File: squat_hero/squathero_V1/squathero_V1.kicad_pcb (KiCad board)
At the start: 2 copper layers, 36.5 x 31.5 mm, 6 parts, among them U2 AMS1117

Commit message: V1 squat hero
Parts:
- removed FB1: ~, PCM_JLCPCB:FB_0805
- added C1: 1uF, Resistor_SMD:R_0805_2012Metric, F.Cu at (148.9, 115.5)
- added C2: 10nF, Resistor_SMD:R_0805_2012Metric, F.Cu at (146.8, 115.5)
- added C3: 1uF, Resistor_SMD:R_0805_2012Metric, F.Cu at (148.9, 109.8)
- added C4: 1uF, Resistor_SMD:R_0805_2012Metric, F.Cu at (171.1, 94.4)
- added C5: 1uF, Resistor_SMD:R_0805_2012Metric, F.Cu at (166.2, 92.5)
- added D2: Yellow, PCM_JLCPCB:D_0805, F.Cu at (147.4, 122.2)
- added D3: Green, PCM_JLCPCB:D_0805, F.Cu at (167.4, 107.8)
- added D4: Red, PCM_JLCPCB:D_0603, F.Cu at (167.4, 105.8)
- added D5: 1N5819WS, PCM_JLCPCB:D_SOD-323, F.Cu at (160.2, 92.2)
- added D6: 1N5819WS, PCM_JLCPCB:D_SOD-323, F.Cu at (156.0, 96.8)
- added D7: H3V3L10B, PCM_JLCPCB:D_DFN1006-2L, F.Cu at (158.0, 82.2)
- added D8: H3V3L10B, PCM_JLCPCB:D_DFN1006-2L, F.Cu at (158.2, 83.5)
- added FB2: ~, PCM_JLCPCB:FB_0805, F.Cu at (164.0, 92.5)
- added J1: Conn_01x03, Connector_PinSocket_2.54mm:PinSocket_1x03_P2.54mm_Vertical, F.Cu at (132.5, 87.1)
- added J3: Conn_01x02, Connector_PinSocket_2.54mm:PinSocket_1x02_P2.54mm_Vertical, F.Cu at (130.4, 109.4)
- added J4: Conn_01x02, Connector_PinSocket_2.54mm:PinSocket_1x02_P2.54mm_Vertical, F.Cu at (128.2, 99.0)
- added J5: Conn_01x02, Connector_PinSocket_2.54mm:PinSocket_1x02_P2.54mm_Vertical, F.Cu at (155.8, 102.5)
- added Q1: HL2307, PCM_JLCPCB:Q_SOT-23, F.Cu at (135.1, 109.5)
- added Q2: HL2307, PCM_JLCPCB:Q_SOT-23, F.Cu at (132.3, 101.7)
- added Q3: HL2307, PCM_JLCPCB:Q_SOT-23, F.Cu at (159.9, 96.8)
- added R10: 2.5k, Resistor_SMD:R_0805_2012Metric, F.Cu at (164.2, 104.2)
- added R11: 10k, Resistor_SMD:R_0805_2012Metric, F.Cu at (165.3, 96.8)
- added R12: 330, Resistor_SMD:R_0805_2012Metric, F.Cu at (133.2, 93.2)
- added R13: 330, Resistor_SMD:R_0805_2012Metric, F.Cu at (134.5, 91.0)
- added R3: 10k, Resistor_SMD:R_0805_2012Metric, F.Cu at (146.8, 111.8)
- added R4: 4.7k, Resistor_SMD:R_0805_2012Metric, F.Cu at (147.3, 95.2)
- added R5: 4.7k, Resistor_SMD:R_0805_2012Metric, F.Cu at (152.1, 92.6)
- added R6: 10k, Resistor_SMD:R_0805_2012Metric, F.Cu at (139.9, 90.0)
- added R7: 50, Resistor_SMD:R_0805_2012Metric, F.Cu at (152.6, 120.0)
- added R8: 50, Resistor_SMD:R_0805_2012Metric, F.Cu at (147.4, 120.0)
- added R9: 1k, Resistor_SMD:R_0805_2012Metric, F.Cu at (167.4, 110.0)
- added S1: Tactile Button, 160gf, PCM_JLCPCB:SW-SMD_4P-L5.1-W5.1-P3.70-LS6.5-TL-2, F.Cu at (139.8, 84.5)
- added U3: AMS1117-3.3, Package_TO_SOT_SMD:SOT-223-3_TabPin2, F.Cu at (156.0, 111.4)
- added U4: ~, imu:LGA-14_L3.0-W2.5-P0.50-TL_QMI8658A, F.Cu at (150.0, 100.0)
- added U5: TP4057, PCM_JLCPCB:SOT-23-6_L2.9-W1.6-P0.95-LS2.8-BL, F.Cu at (165.5, 100.0)
- added U6: ~, batt_conn:Untitled, F.Cu at (171.0, 100.1)
- D1: value H5VUT1B -> White; footprint PCM_JLCPCB:SOT-143-4_L2.9-W1.3-P1.90-LS2.4-BL-1 -> PCM_JLCPCB:D_0805
- R1, R2: footprint Resistor_SMD:R_0805_2012Metric -> Resistor_SMD:R_0201_0603Metric
- U1: footprint JLCPCB_USB-C:USB-SMD_TYPE-C16PIN-1 -> JLCPCB_USB_FOOTPRINT:USB-SMD_TYPE-C16PIN-1
- U2: value AMS1117 -> ~; footprint PCM_JLCPCB:SOT-223-3_L6.5-W3.4-P2.30-LS7.0-BR -> esp_32:WIFIM-SMD_ESP32-C3-MINI-1
- moved U1 52.3 mm to (164.7, 85.3), turned to 135 degrees
- moved R1 51.8 mm to (169.8, 89.1), turned to -45 degrees
- moved D1 40.2 mm to (152.6, 122.2)
- moved R2 39.9 mm to (169.2, 89.7), turned to -45 degrees
- moved U2 27.0 mm to (150.0, 81.7), turned to 0 degrees
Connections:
- D1 pad 1: /USB_D+ -> Net-(D1-Pad1)
- D1 pad 2: /USB_D- -> /DEBUG_LED1
- U2 pad 2: REG_3.3V -> GND
- U2 pad 3: /+5V -> /+3.3V
- U2 pad 4: REG_3.3V -> unconnected-(U2-NC-Pad4)
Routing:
- net /DEBUG_LED2: track 0.00 -> 56.2 mm, vias 0 -> 2
- net /DEBUG_LED1: track 0.00 -> 55.4 mm, vias 0 -> 2
- net /+5V: track 0.00 -> 39.3 mm
- net /PWM_1: track 0.00 -> 37.0 mm, vias 0 -> 2
- net /PWM_2: track 0.00 -> 36.2 mm, vias 0 -> 2
- net GND: track 0.00 -> 27.4 mm, vias 0 -> 49
- net /+3.3V: track 0.00 -> 25.6 mm, vias 0 -> 13
- net /BATT+: track 0.00 -> 24.2 mm, vias 0 -> 2
- net /I2C_INT1: track 0.00 -> 22.1 mm, vias 0 -> 2
- net /GPI0_10: track 0.00 -> 18.8 mm, vias 0 -> 2
- net /raw_power: track 0.00 -> 18.0 mm
- net /I2C_SCL_1: track 0.00 -> 15.4 mm
- net /I2C_SDA_1: track 0.00 -> 15.3 mm
- net /I2C_INT2: track 0.00 -> 15.1 mm, vias 0 -> 2
- net /GPI0_1: track 0.00 -> 14.0 mm, vias 0 -> 2
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- added copper zone on F.Cu, net /+3.3V
- added copper zone on In2.Cu, net /+3.3V
- added copper zone on In1.Cu, net GND
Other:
- board size 36.5 x 31.5 mm -> 50 x 50 mm
- copper layers 2 -> 4

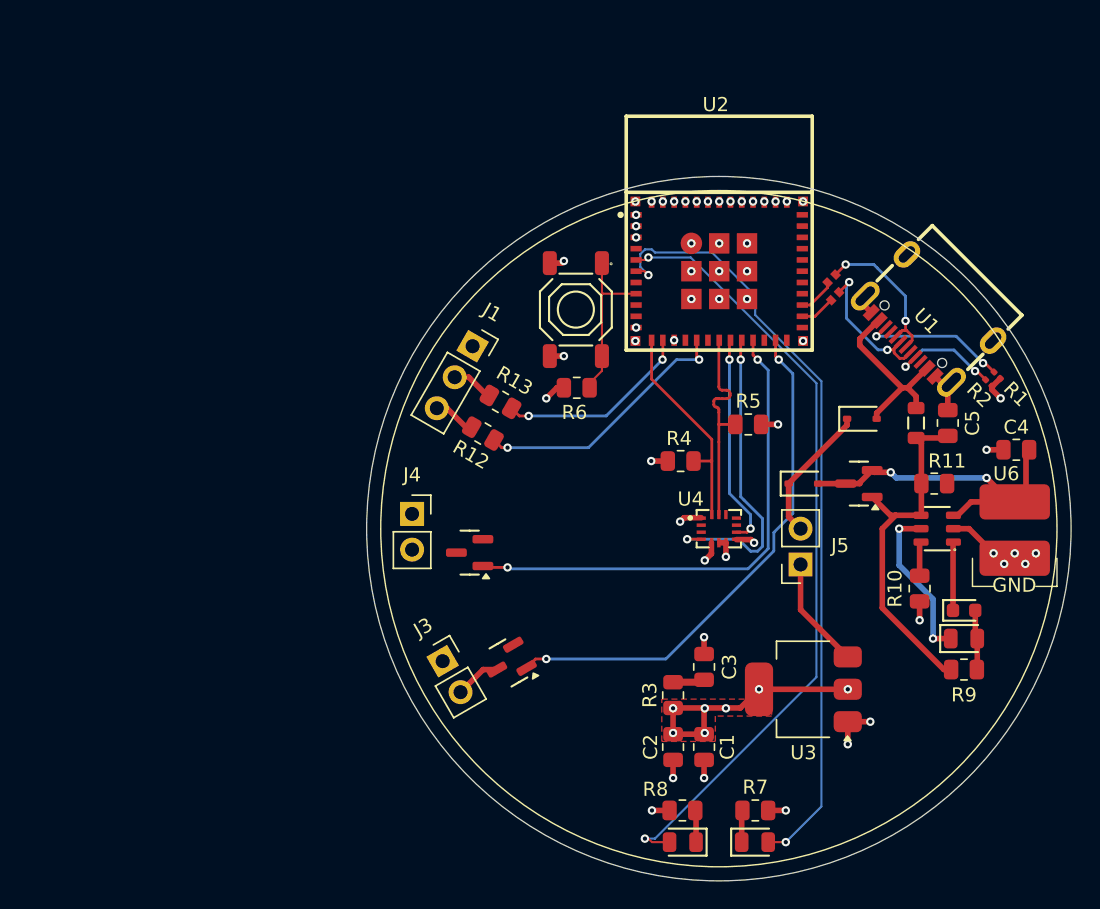
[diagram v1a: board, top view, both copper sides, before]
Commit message: all formatted besides power / BMS
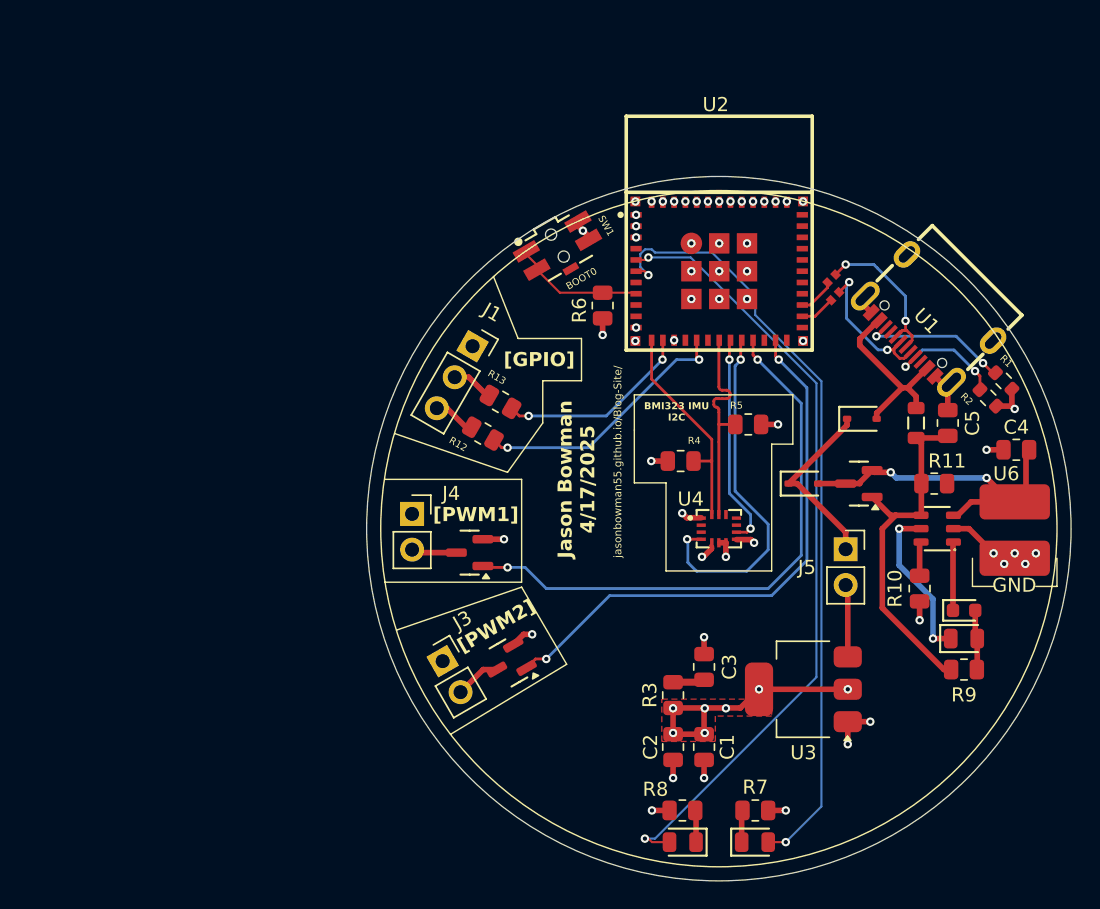
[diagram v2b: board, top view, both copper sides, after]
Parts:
- removed S1: Tactile Button, 160gf, PCM_JLCPCB:SW-SMD_4P-L5.1-W5.1-P3.70-LS6.5-TL-2
- added SW1: ~, Button_Switch_SMD:SW-SMD_4P-L3.5-W3.5_PTS840GKPSMTRLFS, F.Cu at (138.8, 80.4)
- R1, R2: footprint Resistor_SMD:R_0201_0603Metric -> Resistor_SMD:R_0603_1608Metric
- moved R6 6.12 mm to (141.8, 84.2), turned to 90 degrees
- moved J5 3.38 mm to (159.0, 101.5), turned to 0 degrees
- moved R2 1.06 mm to (169.1, 90.7)
- moved R1 0.62 mm to (170.2, 89.5)
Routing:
- net /PWM_2: track 36.2 -> 40.9 mm
- net Net-(J4-Pin_2): track 0.00 -> 3.23 mm
- net /I2C_INT1: track 22.1 -> 25.3 mm
- net /PWM_1: track 37.0 -> 39.6 mm
- net /+3.3V: track 25.6 -> 28.0 mm, vias 13 -> 15
- net /EN: track 11.7 -> 9.36 mm
- net /CC1: track 8.05 -> 8.64 mm
- net GND: track 27.4 -> 27.5 mm, vias 49 -> 48
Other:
- board text added: "BMI323 IMU I2C"
- board text added: "BOOT0"
- board text added: "Jason Bowman 4/17/2025"
- board text added: "[GPIO]"
- board text added: "[PWM1]"
- board text added: "[PWM2]"
- board text added: "jasonbowman55.github.io/Blog-Site/"
